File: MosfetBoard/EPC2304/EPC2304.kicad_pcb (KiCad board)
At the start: 2 copper layers, 120 x 75 mm, 179 parts, among them J10 DriverConn, J14 BATT-Conn2, J4 PhaseConn, J5 PhaseConn, J6 PhaseConn, J7 DriverConn, J8 DriverConn, J9 BATT-Conn1, Q1 EPC2304, Q13 EPC2304, Q14 EPC2304, Q15 EPC2304, Q2 EPC2304, Q3 EPC2304, Q4 EPC2304, Q5 EPC2304, Q6 EPC2304, Q7 EPC2304, Q8 EPC2304, Q9 EPC2304, U1 2EDF7275KXUMA1, U2 2EDF7275KXUMA1, U3 2EDF7275KXUMA1

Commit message: v2.6.2 - EPC2304
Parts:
- removed JP1, JP2, JP3: DummyJumper, GigaVescLibs:SolderJumper0.3mm
- added U10: INA181, Package_TO_SOT_SMD:SOT-23-6, F.Cu at (208.2, 108.2)
- added U11: INA181, Package_TO_SOT_SMD:SOT-23-6, F.Cu at (162.5, 108.2)
- added U12: INA181, Package_TO_SOT_SMD:SOT-23-6, F.Cu at (116.8, 108.2)
- R17, R18, R19, R28, R29, R30: footprint Resistor_SMD:R_1218_3246Metric_Pad1.22x4.75mm_HandSolder -> Resistor_SMD:R_2512_6332Metric
- moved C37 20.4 mm to (195.2, 101.0), turned to 180 degrees
- moved C38 20.4 mm to (149.5, 101.0), turned to 180 degrees
- moved C43 20.4 mm to (103.8, 101.0), turned to 180 degrees
- moved TH1 20.0 mm to (195.2, 99.5), turned to 0 degrees
- moved TH2 20.0 mm to (149.5, 99.5), turned to 0 degrees
- moved TH3 20.0 mm to (103.8, 99.5), turned to 0 degrees
- moved R15 18.5 mm to (103.8, 102.5), turned to 180 degrees
- moved R3 18.5 mm to (195.2, 102.5), turned to 180 degrees
- moved R4 18.5 mm to (149.5, 102.5), turned to 180 degrees
- moved R17 15.4 mm to (209.8, 103.2)
- moved R18 15.4 mm to (164.0, 103.2)
- moved R19 15.4 mm to (118.2, 103.2)
- moved C13 13.3 mm to (161.5, 60.8), turned to -90 degrees
- moved C17 13.3 mm to (115.8, 60.8), turned to -90 degrees
- moved C5 13.3 mm to (207.2, 60.8), turned to -90 degrees
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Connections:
- C14 pad 1: /PhaseMosfets2/3.3V_IN -> -BATT
- C14 pad 2: -BATT -> /PhaseMosfets2/3.3V_IN
- C18 pad 1: /PhaseMosfets3/3.3V_IN -> -BATT
- C18 pad 2: -BATT -> /PhaseMosfets3/3.3V_IN
- C6 pad 1: /PhaseMosfets1/3.3V_IN -> -BATT
- C6 pad 2: -BATT -> /PhaseMosfets1/3.3V_IN
- J4 pad 3: /PhaseMosfets1/SH- -> -BATT
- J5 pad 3: /PhaseMosfets2/SH- -> -BATT
- J6 pad 3: /PhaseMosfets3/SH- -> -BATT
- Q4 pad 2: /PhaseMosfets1/SH+ -> -BATT
- Q4 pad 4: /PhaseMosfets1/SH+ -> -BATT
- Q4 pad 6: /PhaseMosfets1/SH+ -> -BATT
- Q5 pad 2: /PhaseMosfets2/SH+ -> -BATT
- Q5 pad 4: /PhaseMosfets2/SH+ -> -BATT
- Q5 pad 6: /PhaseMosfets2/SH+ -> -BATT
- Q6 pad 2: /PhaseMosfets3/SH+ -> -BATT
- Q6 pad 4: /PhaseMosfets3/SH+ -> -BATT
- Q6 pad 6: /PhaseMosfets3/SH+ -> -BATT
- Q7 pad 2: /PhaseMosfets1/SH+ -> -BATT
- Q7 pad 4: /PhaseMosfets1/SH+ -> -BATT
- Q7 pad 6: /PhaseMosfets1/SH+ -> -BATT
- Q8 pad 2: /PhaseMosfets2/SH+ -> -BATT
- Q8 pad 4: /PhaseMosfets2/SH+ -> -BATT
- Q8 pad 6: /PhaseMosfets2/SH+ -> -BATT
- Q9 pad 2: /PhaseMosfets3/SH+ -> -BATT
- Q9 pad 4: /PhaseMosfets3/SH+ -> -BATT
- Q9 pad 6: /PhaseMosfets3/SH+ -> -BATT
- R17 pad 1: /PhaseMosfets1/SH+ -> /PhaseMosfets1/PHASE
- R17 pad 2: -BATT -> Net-(U10-+)
- R18 pad 1: /PhaseMosfets2/SH+ -> /PhaseMosfets2/PHASE
- R18 pad 2: -BATT -> Net-(U11-+)
- R19 pad 1: /PhaseMosfets3/SH+ -> /PhaseMosfets3/PHASE
- R19 pad 2: -BATT -> Net-(U12-+)
- R28 pad 1: /PhaseMosfets1/SH+ -> /PhaseMosfets1/PHASE
- R28 pad 2: -BATT -> Net-(U10-+)
- R29 pad 1: /PhaseMosfets2/SH+ -> /PhaseMosfets2/PHASE
- R29 pad 2: -BATT -> Net-(U11-+)
- R30 pad 1: /PhaseMosfets3/SH+ -> /PhaseMosfets3/PHASE
- R30 pad 2: -BATT -> Net-(U12-+)
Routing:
- net /PhaseMosfets3/3.3V_IN2: track 0.00 -> 35.3 mm
- net /PhaseMosfets3/PL: track 24.3 -> 3.41 mm
- net /PhaseMosfets3/12V_IN: track 15.9 -> 0.00 mm
- net -BATT: track 15.1 -> 0.00 mm
- net Net-(D15-A): track 1.38 -> 15.5 mm, vias 0 -> 2
- net /PhaseMosfets3/MOS_TEMP: track 0.00 -> 11.2 mm
- net /PhaseMosfets3/H: track 10.7 -> 0.00 mm
- net /PhaseMosfets3/DISABLE: track 10.7 -> 0.00 mm
- net /PhaseMosfets3/SH+: track 0.00 -> 9.76 mm
- net /PhaseMosfets3/3.3V_IN: track 7.52 -> 0.00 mm
- net Net-(D9-A): track 1.38 -> 7.52 mm, vias 0 -> 2
- net /PhaseMosfets3/V_SENSE: track 0.00 -> 6.10 mm
- net /PhaseMosfets3/L: track 5.74 -> 0.00 mm
- net Net-(D7-K): track 5.25 -> 0.00 mm
- net /PhaseMosfets3/PH: track 7.98 -> 4.00 mm
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- added copper zone on F.Cu, net Net-(U12-+)
- removed copper zone on F.Cu, net /PhaseMosfets3/SH+

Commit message: v2.7.0 - Phase shunts
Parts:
- removed U10, U11, U12: INA181, Package_TO_SOT_SMD:SOT-23-6
- added D16: 3.3V, Diode_SMD:D_MicroMELF, F.Cu at (192.5, 99.0)
- added D17: 3.3V, Diode_SMD:D_MicroMELF, F.Cu at (146.8, 99.0)
- added D18: 3.3V, Diode_SMD:D_MicroMELF, F.Cu at (101.0, 99.0)
- added R11: 10, Resistor_SMD:R_0603_1608Metric, F.Cu at (199.8, 101.5)
- added R12: 10, Resistor_SMD:R_0603_1608Metric, F.Cu at (154.0, 101.5)
- added R16: 10, Resistor_SMD:R_0603_1608Metric, F.Cu at (108.2, 101.5)
- added R31: 10, Resistor_SMD:R_0603_1608Metric, F.Cu at (189.5, 99.0)
- added R32: 10, Resistor_SMD:R_0603_1608Metric, F.Cu at (143.8, 99.0)
- added R33: 10, Resistor_SMD:R_0603_1608Metric, F.Cu at (98.0, 99.0)
- added U4: AMC1301DWVR, Package_SO:SOIC-8_7.5x5.85mm_P1.27mm, F.Cu at (191.5, 106.5)
- added U5: AMC1301DWVR, Package_SO:SOIC-8_7.5x5.85mm_P1.27mm, F.Cu at (145.8, 106.5)
- added U6: AMC1301DWVR, Package_SO:SOIC-8_7.5x5.85mm_P1.27mm, F.Cu at (100.0, 106.5)
- moved C37 1.60 mm to (196.2, 102.2)
- moved C38 1.60 mm to (150.5, 102.2)
- moved C43 1.60 mm to (104.8, 102.2)
- moved R15 1.60 mm to (104.8, 103.8)
- moved R3 1.60 mm to (196.2, 103.8)
- moved R4 1.60 mm to (150.5, 103.8)
- moved TH1 1.60 mm to (196.2, 100.8)
- moved TH2 1.60 mm to (150.5, 100.8)
- moved TH3 1.60 mm to (104.8, 100.8)
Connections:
- C15 pad 2: /PhaseMosfets2/PHASE -> GNDREF
- C19 pad 2: /PhaseMosfets3/PHASE -> GNDREF
- C7 pad 2: /PhaseMosfets1/PHASE -> GNDREF
- J4 pad 3: -BATT -> /PhaseMosfets1/SH-
- J5 pad 3: -BATT -> /PhaseMosfets2/SH-
- J6 pad 3: -BATT -> /PhaseMosfets3/SH-
- Q1 pad 2: /PhaseMosfets1/PHASE -> GNDREF
- Q1 pad 4: /PhaseMosfets1/PHASE -> GNDREF
- Q1 pad 6: /PhaseMosfets1/PHASE -> GNDREF
- Q13 pad 2: /PhaseMosfets1/PHASE -> GNDREF
- Q13 pad 4: /PhaseMosfets1/PHASE -> GNDREF
- Q13 pad 6: /PhaseMosfets1/PHASE -> GNDREF
- Q14 pad 2: /PhaseMosfets2/PHASE -> GNDREF
- Q14 pad 4: /PhaseMosfets2/PHASE -> GNDREF
- Q14 pad 6: /PhaseMosfets2/PHASE -> GNDREF
- Q15 pad 2: /PhaseMosfets3/PHASE -> GNDREF
- Q15 pad 4: /PhaseMosfets3/PHASE -> GNDREF
- Q15 pad 6: /PhaseMosfets3/PHASE -> GNDREF
- Q2 pad 2: /PhaseMosfets2/PHASE -> GNDREF
- Q2 pad 4: /PhaseMosfets2/PHASE -> GNDREF
- Q2 pad 6: /PhaseMosfets2/PHASE -> GNDREF
- Q3 pad 2: /PhaseMosfets3/PHASE -> GNDREF
- Q3 pad 4: /PhaseMosfets3/PHASE -> GNDREF
- Q3 pad 6: /PhaseMosfets3/PHASE -> GNDREF
- Q4 pad 3: /PhaseMosfets1/PHASE -> GNDREF
- Q4 pad 5: /PhaseMosfets1/PHASE -> GNDREF
- Q4 pad 7: /PhaseMosfets1/PHASE -> GNDREF
- Q5 pad 3: /PhaseMosfets2/PHASE -> GNDREF
- Q5 pad 5: /PhaseMosfets2/PHASE -> GNDREF
- Q5 pad 7: /PhaseMosfets2/PHASE -> GNDREF
- Q6 pad 3: /PhaseMosfets3/PHASE -> GNDREF
- Q6 pad 5: /PhaseMosfets3/PHASE -> GNDREF
- Q6 pad 7: /PhaseMosfets3/PHASE -> GNDREF
- Q7 pad 3: /PhaseMosfets1/PHASE -> GNDREF
- Q7 pad 5: /PhaseMosfets1/PHASE -> GNDREF
- Q7 pad 7: /PhaseMosfets1/PHASE -> GNDREF
- Q8 pad 3: /PhaseMosfets2/PHASE -> GNDREF
- Q8 pad 5: /PhaseMosfets2/PHASE -> GNDREF
- Q8 pad 7: /PhaseMosfets2/PHASE -> GNDREF
- Q9 pad 3: /PhaseMosfets3/PHASE -> GNDREF
- Q9 pad 5: /PhaseMosfets3/PHASE -> GNDREF
- Q9 pad 7: /PhaseMosfets3/PHASE -> GNDREF
- R1 pad 1: /PhaseMosfets1/PHASE -> GNDREF
- R13 pad 1: /PhaseMosfets2/PHASE -> GNDREF
- R17 pad 1: /PhaseMosfets1/PHASE -> GNDREF
- R18 pad 1: /PhaseMosfets2/PHASE -> GNDREF
- R19 pad 1: /PhaseMosfets3/PHASE -> GNDREF
- R20 pad 1: /PhaseMosfets3/PHASE -> GNDREF
- R27 pad 1: /PhaseMosfets1/PHASE -> GNDREF
- R28 pad 1: /PhaseMosfets1/PHASE -> GNDREF
- R29 pad 1: /PhaseMosfets2/PHASE -> GNDREF
- R30 pad 1: /PhaseMosfets3/PHASE -> GNDREF
- R40 pad 1: /PhaseMosfets2/PHASE -> GNDREF
- R47 pad 1: /PhaseMosfets3/PHASE -> GNDREF
- U1 pad 11: /PhaseMosfets1/PHASE -> GNDREF
- U2 pad 11: /PhaseMosfets2/PHASE -> GNDREF
- U3 pad 11: /PhaseMosfets3/PHASE -> GNDREF
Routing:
- net /PhaseMosfets3/3.3V_IN2: track 35.3 -> 5.80 mm
- net /PhaseMosfets3/SH-: track 0.00 -> 12.6 mm
- net GNDREF: track 0.00 -> 2.65 mm
- net /PhaseMosfets3/PHASE: track 2.65 -> 0.00 mm
- net /PhaseMosfets3/MOS_TEMP: track 11.2 -> 10.1 mm
- net /PhaseMosfets3/SH+: track 9.76 -> 10.3 mm
- added copper zone on F.Cu, net GNDREF
- removed copper zone on F.Cu, net /PhaseMosfets3/PHASE

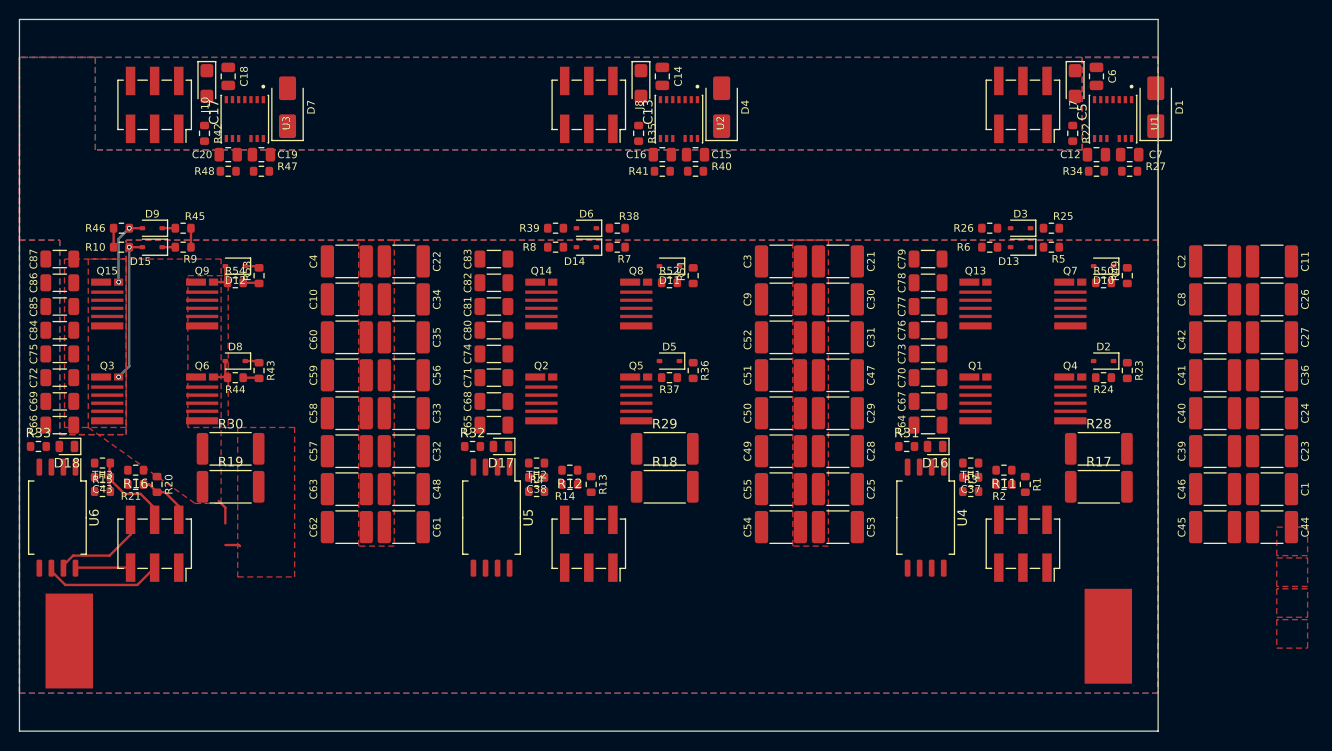
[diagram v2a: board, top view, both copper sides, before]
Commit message: v2.8.0 - Small Hall sensors
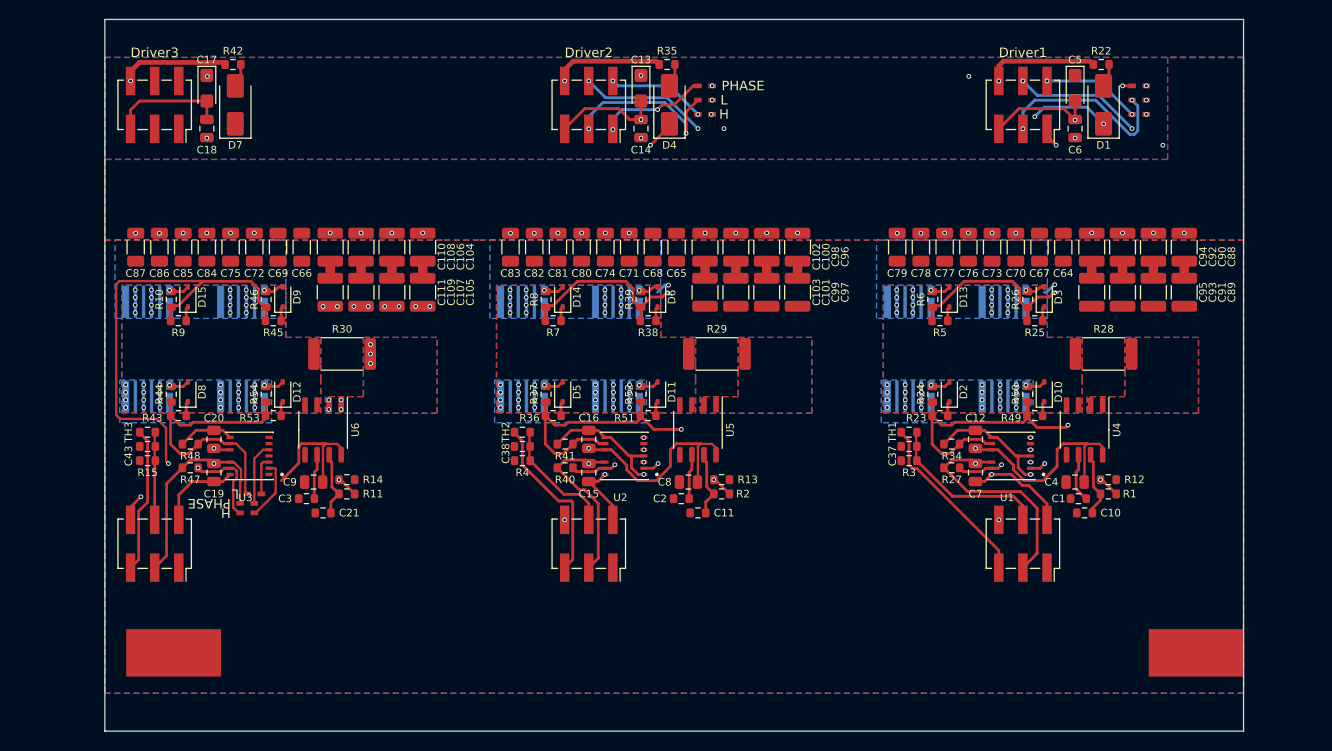
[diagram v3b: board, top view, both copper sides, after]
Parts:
- removed C22, C23, C24, C25, C26, C27, C28, C29, C30, C31, C32, C33, C34, C35, C36, C39, C40, C41, C42, C44, C45, C46, C47, C48, C49, C50, C51, C52, C53, C54, C55, C56, C57, C58, C59, C60, C61, C62, C63: 1u 200V, Capacitor_SMD:C_1812_4532Metric
- removed D16, D17, D18: 3.3V, Diode_SMD:D_MicroMELF
- removed R16, R31, R32, R33: 10, Resistor_SMD:R_0603_1608Metric
- removed R17, R18, R19: 0.5m, Resistor_SMD:R_2512_6332Metric
- removed R20: 150k, Resistor_SMD:R_0603_1608Metric
- removed R21: 2.7k, Resistor_SMD:R_0603_1608Metric
- added C100: 10u 100V, Capacitor_SMD:C_1210_3225Metric, F.Cu at (171.5, 78.0)
- added C101: 10u 100V, Capacitor_SMD:C_1210_3225Metric, F.Cu at (171.5, 82.8)
- added C102: 10u 100V, Capacitor_SMD:C_1210_3225Metric, F.Cu at (168.2, 78.0)
- added C103: 10u 100V, Capacitor_SMD:C_1210_3225Metric, F.Cu at (168.2, 82.8)
- added C104: 10u 100V, Capacitor_SMD:C_1210_3225Metric, F.Cu at (138.5, 78.0)
- added C105: 10u 100V, Capacitor_SMD:C_1210_3225Metric, F.Cu at (138.5, 82.8)
- added C106: 10u 100V, Capacitor_SMD:C_1210_3225Metric, F.Cu at (135.2, 78.0)
- added C107: 10u 100V, Capacitor_SMD:C_1210_3225Metric, F.Cu at (135.2, 82.8)
- added C108: 10u 100V, Capacitor_SMD:C_1210_3225Metric, F.Cu at (132.0, 78.0)
- added C109: 10u 100V, Capacitor_SMD:C_1210_3225Metric, F.Cu at (132.0, 82.8)
- added C110: 10u 100V, Capacitor_SMD:C_1210_3225Metric, F.Cu at (128.8, 78.0)
- added C111: 10u 100V, Capacitor_SMD:C_1210_3225Metric, F.Cu at (128.8, 82.8)
- added C88: 10u 100V, Capacitor_SMD:C_1210_3225Metric, F.Cu at (218.8, 78.0)
- added C89: 10u 100V, Capacitor_SMD:C_1210_3225Metric, F.Cu at (218.8, 82.8)
- added C90: 10u 100V, Capacitor_SMD:C_1210_3225Metric, F.Cu at (215.5, 78.0)
- added C91: 10u 100V, Capacitor_SMD:C_1210_3225Metric, F.Cu at (215.5, 82.8)
- added C92: 10u 100V, Capacitor_SMD:C_1210_3225Metric, F.Cu at (212.2, 78.0)
- added C93: 10u 100V, Capacitor_SMD:C_1210_3225Metric, F.Cu at (212.2, 82.8)
- added C94: 10u 100V, Capacitor_SMD:C_1210_3225Metric, F.Cu at (209.0, 78.0)
- added C95: 10u 100V, Capacitor_SMD:C_1210_3225Metric, F.Cu at (209.0, 82.8)
- added C96: 10u 100V, Capacitor_SMD:C_1210_3225Metric, F.Cu at (178.0, 78.0)
- added C97: 10u 100V, Capacitor_SMD:C_1210_3225Metric, F.Cu at (178.0, 82.8)
- added C98: 10u 100V, Capacitor_SMD:C_1210_3225Metric, F.Cu at (174.8, 78.0)
- added C99: 10u 100V, Capacitor_SMD:C_1210_3225Metric, F.Cu at (174.8, 82.8)
- added JP1: DirectJump, GigaVescLibs:SolderJumper0.5mm_Open, F.Cu at (214.0, 61.0)
- added JP10: DirectJump, GigaVescLibs:SolderJumper0.5mm_Open, F.Cu at (120.8, 104.0)
- added JP11: DirectJump, GigaVescLibs:SolderJumper0.5mm_Open, F.Cu at (120.0, 106.0)
- added JP2: DirectJump, GigaVescLibs:SolderJumper0.5mm_Open, F.Cu at (214.0, 62.5)
- added JP3: DirectJump, GigaVescLibs:SolderJumper0.5mm_Open, F.Cu at (214.0, 64.0)
- added JP5: DirectJump, GigaVescLibs:SolderJumper0.5mm_Open, F.Cu at (168.2, 61.0)
- added JP6: DirectJump, GigaVescLibs:SolderJumper0.5mm_Open, F.Cu at (168.2, 62.5)
- added JP7: DirectJump, GigaVescLibs:SolderJumper0.5mm_Open, F.Cu at (168.2, 64.0)
- added JP9: DirectJump, GigaVescLibs:SolderJumper0.5mm_Open, F.Cu at (120.0, 105.0)
- C1, C2, C3: value 1u 200V -> 10n; footprint Capacitor_SMD:C_1812_4532Metric -> GigaVescLibs:C_0603_1608Metric_L
- C10, C11, C21: value 1u 200V -> 1n; footprint Capacitor_SMD:C_1812_4532Metric -> GigaVescLibs:C_0603_1608Metric_L
- C4, C8, C9: value 1u 200V -> 100n; footprint Capacitor_SMD:C_1812_4532Metric -> Capacitor_SMD:C_0805_2012Metric
- Q1, Q13, Q14, Q15, Q2, Q3, Q4, Q5, Q6, Q7, Q8, Q9: moved to B.Cu
- R1: value 150k -> 4.7k
- R11: value 10 -> 4.7k
- R12: value 10 -> 9.1k
- R13: value 150k -> 9.1k
- R14: value 2.7k -> 9.1k
- R2: value 2.7k -> 4.7k
- R28, R29, R30: value 0.5m -> 0.3m
- U4, U5, U6: value AMC1301DWVR -> MT9223CT-50BR5; footprint Package_SO:SOIC-8_7.5x5.85mm_P1.27mm -> Package_SO:SOP-8_3.9x4.9mm_P1.27mm
- moved C10 80.9 mm to (208.2, 106.0)
- moved C4 80.2 mm to (207.2, 102.8), turned to 0 degrees
- moved R11 69.3 mm to (130.5, 104.0)
- moved C11 66.0 mm to (167.5, 106.0), turned to 180 degrees
- moved C2 61.6 mm to (165.8, 104.5)
- moved C21 60.4 mm to (128.0, 106.0), turned to 180 degrees
- moved C8 58.7 mm to (166.5, 102.8), turned to 0 degrees
- moved R12 56.8 mm to (210.8, 102.5)
- moved C3 55.9 mm to (126.2, 104.5)
- moved C9 52.9 mm to (127.0, 102.8), turned to 0 degrees
- moved C7 37.2 mm to (196.8, 101.8), turned to 90 degrees
- moved U1 37.1 mm to (200.5, 100.0), turned to 180 degrees
- moved R27 36.4 mm to (194.2, 101.2)
- moved U2 36.0 mm to (159.8, 100.0), turned to 180 degrees
- moved U3 35.5 mm to (120.2, 100.0), turned to 180 degrees
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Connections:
- C1 pad 1: +BATT -> Net-(U4-FILTER)
- C1 pad 2: -BATT -> GNDA
- C10 pad 1: +BATT -> Net-(U4-VIOUT)
- C10 pad 2: -BATT -> GNDA
- C11 pad 1: +BATT -> Net-(U5-VIOUT)
- C11 pad 2: -BATT -> GNDA
- C12 pad 1: /PhaseMosfets1/12V_IN -> /PhaseMosfets1/DRV_POWER
- C12 pad 2: /PhaseMosfets1/PHASE_GROUND -> -BATT
- C15 pad 1: Net-(D4-K) -> /PhaseMosfets2/FLOAT_VDD
- C15 pad 2: GNDREF -> /PhaseMosfets2/PHASE
- C16 pad 1: /PhaseMosfets2/12V_IN -> /PhaseMosfets2/DRV_POWER
- C16 pad 2: /PhaseMosfets2/PHASE_GROUND -> -BATT
- C19 pad 1: Net-(D7-K) -> /PhaseMosfets3/FLOAT_VDD
- C19 pad 2: GNDREF -> /PhaseMosfets3/PHASE
- C2 pad 1: +BATT -> Net-(U5-FILTER)
- C2 pad 2: -BATT -> GNDA
- C20 pad 1: /PhaseMosfets3/12V_IN -> /PhaseMosfets3/DRV_POWER
- C20 pad 2: /PhaseMosfets3/PHASE_GROUND -> -BATT
- C21 pad 1: +BATT -> Net-(U6-VIOUT)
- C21 pad 2: -BATT -> GNDA
- C3 pad 1: +BATT -> Net-(U6-FILTER)
- C3 pad 2: -BATT -> GNDA
- C4 pad 1: +BATT -> -BATT
- C4 pad 2: -BATT -> /PhaseMosfets1/DRV_POWER
- C7 pad 1: Net-(D1-K) -> /PhaseMosfets1/FLOAT_VDD
- C7 pad 2: GNDREF -> /PhaseMosfets1/PHASE
- C8 pad 1: +BATT -> -BATT
- C8 pad 2: -BATT -> /PhaseMosfets2/DRV_POWER
- C9 pad 1: +BATT -> -BATT
- C9 pad 2: -BATT -> /PhaseMosfets3/DRV_POWER
- D1 pad 1: Net-(D1-K) -> /PhaseMosfets1/FLOAT_VDD
- D4 pad 1: Net-(D4-K) -> /PhaseMosfets2/FLOAT_VDD
- D7 pad 1: Net-(D7-K) -> /PhaseMosfets3/FLOAT_VDD
- J10 pad 1: -BATT -> /PhaseMosfets3/LOCKOUT
- J10 pad 4: /PhaseMosfets3/DISABLE -> -BATT
- J10 pad 6: /PhaseMosfets3/12V_IN -> /PhaseMosfets3/DRV_POWER
- J4 pad 2: /PhaseMosfets1/V_SENSE -> /PhaseMosfets1/FLOAT_VDD
- J4 pad 3: /PhaseMosfets1/SH- -> GNDA
- J5 pad 2: /PhaseMosfets2/V_SENSE -> /PhaseMosfets2/FLOAT_VDD
- J5 pad 3: /PhaseMosfets2/SH- -> GNDA
- J6 pad 2: /PhaseMosfets3/V_SENSE -> /PhaseMosfets3/FLOAT_VDD
- J6 pad 3: /PhaseMosfets3/SH- -> GNDA
- J7 pad 1: -BATT -> /PhaseMosfets1/LOCKOUT
- J7 pad 4: /PhaseMosfets1/DISABLE -> -BATT
- J7 pad 6: /PhaseMosfets1/12V_IN -> /PhaseMosfets1/DRV_POWER
- J8 pad 1: -BATT -> /PhaseMosfets2/LOCKOUT
- J8 pad 4: /PhaseMosfets2/DISABLE -> -BATT
- J8 pad 6: /PhaseMosfets2/12V_IN -> /PhaseMosfets2/DRV_POWER
- Q1 pad 2: GNDREF -> /PhaseMosfets1/PHASE
- Q1 pad 4: GNDREF -> /PhaseMosfets1/PHASE
- Q1 pad 6: GNDREF -> /PhaseMosfets1/PHASE
- Q13 pad 2: GNDREF -> /PhaseMosfets1/PHASE
- Q13 pad 4: GNDREF -> /PhaseMosfets1/PHASE
- Q13 pad 6: GNDREF -> /PhaseMosfets1/PHASE
- Q14 pad 2: GNDREF -> /PhaseMosfets2/PHASE
- Q14 pad 4: GNDREF -> /PhaseMosfets2/PHASE
- Q14 pad 6: GNDREF -> /PhaseMosfets2/PHASE
- Q15 pad 2: GNDREF -> /PhaseMosfets3/PHASE
- Q15 pad 4: GNDREF -> /PhaseMosfets3/PHASE
- Q15 pad 6: GNDREF -> /PhaseMosfets3/PHASE
- Q2 pad 2: GNDREF -> /PhaseMosfets2/PHASE
- Q2 pad 4: GNDREF -> /PhaseMosfets2/PHASE
- Q2 pad 6: GNDREF -> /PhaseMosfets2/PHASE
- Q3 pad 2: GNDREF -> /PhaseMosfets3/PHASE
- Q3 pad 4: GNDREF -> /PhaseMosfets3/PHASE
- Q3 pad 6: GNDREF -> /PhaseMosfets3/PHASE
- Q4 pad 3: GNDREF -> /PhaseMosfets1/PHASE
- Q4 pad 5: GNDREF -> /PhaseMosfets1/PHASE
- Q4 pad 7: GNDREF -> /PhaseMosfets1/PHASE
- Q5 pad 3: GNDREF -> /PhaseMosfets2/PHASE
- Q5 pad 5: GNDREF -> /PhaseMosfets2/PHASE
- Q5 pad 7: GNDREF -> /PhaseMosfets2/PHASE
- Q6 pad 3: GNDREF -> /PhaseMosfets3/PHASE
- Q6 pad 5: GNDREF -> /PhaseMosfets3/PHASE
- Q6 pad 7: GNDREF -> /PhaseMosfets3/PHASE
- Q7 pad 3: GNDREF -> /PhaseMosfets1/PHASE
- Q7 pad 5: GNDREF -> /PhaseMosfets1/PHASE
- Q7 pad 7: GNDREF -> /PhaseMosfets1/PHASE
- Q8 pad 3: GNDREF -> /PhaseMosfets2/PHASE
- Q8 pad 5: GNDREF -> /PhaseMosfets2/PHASE
- Q8 pad 7: GNDREF -> /PhaseMosfets2/PHASE
- Q9 pad 3: GNDREF -> /PhaseMosfets3/PHASE
- Q9 pad 5: GNDREF -> /PhaseMosfets3/PHASE
- Q9 pad 7: GNDREF -> /PhaseMosfets3/PHASE
- R1 pad 1: GNDREF -> /PhaseMosfets1/SH+
- R1 pad 2: /PhaseMosfets1/V_SENSE -> Net-(U4-VIOUT)
- R11 pad 1: Net-(R11-Pad1) -> /PhaseMosfets3/SH+
- R11 pad 2: Net-(R11-Pad2) -> Net-(U6-VIOUT)
- R12 pad 1: Net-(R12-Pad1) -> GNDA
- R12 pad 2: Net-(R12-Pad2) -> /PhaseMosfets1/SH+
- R13 pad 1: GNDREF -> GNDA
- R13 pad 2: /PhaseMosfets2/V_SENSE -> /PhaseMosfets2/SH+
- R14 pad 1: /PhaseMosfets2/V_SENSE -> GNDA
- R14 pad 2: -BATT -> /PhaseMosfets3/SH+
- R2 pad 1: /PhaseMosfets1/V_SENSE -> /PhaseMosfets2/SH+
- R2 pad 2: -BATT -> Net-(U5-VIOUT)
- R22 pad 1: /PhaseMosfets1/12V_IN -> /PhaseMosfets1/DRV_POWER
- R27 pad 1: GNDREF -> /PhaseMosfets1/PHASE
- R28 pad 1: GNDREF -> /PhaseMosfets1/PHASE
- R28 pad 2: Net-(R11-Pad1) -> Net-(R28-Pad2)
- R29 pad 1: GNDREF -> /PhaseMosfets2/PHASE
- R29 pad 2: Net-(R12-Pad1) -> Net-(R29-Pad2)
- R30 pad 1: GNDREF -> /PhaseMosfets3/PHASE
- R30 pad 2: Net-(R16-Pad1) -> Net-(R30-Pad2)
- R34 pad 1: /PhaseMosfets1/PHASE_GROUND -> -BATT
- R35 pad 1: /PhaseMosfets2/12V_IN -> /PhaseMosfets2/DRV_POWER
- R40 pad 1: GNDREF -> /PhaseMosfets2/PHASE
- R41 pad 1: /PhaseMosfets2/PHASE_GROUND -> -BATT
- R42 pad 1: /PhaseMosfets3/12V_IN -> /PhaseMosfets3/DRV_POWER
- R47 pad 1: GNDREF -> /PhaseMosfets3/PHASE
- R48 pad 1: /PhaseMosfets3/PHASE_GROUND -> -BATT
- U1 pad 10: /PhaseMosfets1/12V_IN -> /PhaseMosfets1/DRV_POWER
- U1 pad 11: GNDREF -> /PhaseMosfets1/PHASE
- U1 pad 13: Net-(D1-K) -> /PhaseMosfets1/FLOAT_VDD
- U1 pad 5: /PhaseMosfets1/DISABLE -> /PhaseMosfets1/LOCKOUT
- U1 pad 8: /PhaseMosfets1/PHASE_GROUND -> -BATT
- U2 pad 10: /PhaseMosfets2/12V_IN -> /PhaseMosfets2/DRV_POWER
- U2 pad 11: GNDREF -> /PhaseMosfets2/PHASE
- U2 pad 13: Net-(D4-K) -> /PhaseMosfets2/FLOAT_VDD
- U2 pad 5: /PhaseMosfets2/DISABLE -> /PhaseMosfets2/LOCKOUT
- U2 pad 8: /PhaseMosfets2/PHASE_GROUND -> -BATT
- U3 pad 10: /PhaseMosfets3/12V_IN -> /PhaseMosfets3/DRV_POWER
- U3 pad 11: GNDREF -> /PhaseMosfets3/PHASE
- U3 pad 13: Net-(D7-K) -> /PhaseMosfets3/FLOAT_VDD
- U3 pad 5: /PhaseMosfets3/DISABLE -> /PhaseMosfets3/LOCKOUT
- U3 pad 8: /PhaseMosfets3/PHASE_GROUND -> -BATT
- U4 pad 1: Net-(D16-K) -> Net-(R28-Pad2)
- U4 pad 2: Net-(R11-Pad2) -> Net-(R28-Pad2)
- U4 pad 3: Net-(R31-Pad2) -> /PhaseMosfets1/PHASE
- U4 pad 4: GNDREF -> /PhaseMosfets1/PHASE
- U4 pad 5: -BATT -> GNDA
- U4 pad 6: /PhaseMosfets1/SH- -> Net-(U4-FILTER)
- U4 pad 7: /PhaseMosfets1/SH+ -> Net-(U4-VIOUT)
- U4 pad 8: /PhaseMosfets1/3.3V_IN2 -> /PhaseMosfets1/DRV_POWER
- U5 pad 1: Net-(D17-K) -> Net-(R29-Pad2)
- U5 pad 2: Net-(R12-Pad2) -> Net-(R29-Pad2)
- U5 pad 3: Net-(R32-Pad2) -> /PhaseMosfets2/PHASE
- U5 pad 4: GNDREF -> /PhaseMosfets2/PHASE
- U5 pad 5: -BATT -> GNDA
- U5 pad 6: /PhaseMosfets2/SH- -> Net-(U5-FILTER)
- U5 pad 7: /PhaseMosfets2/SH+ -> Net-(U5-VIOUT)
- U5 pad 8: /PhaseMosfets2/3.3V_IN2 -> /PhaseMosfets2/DRV_POWER
- U6 pad 1: Net-(D18-K) -> Net-(R30-Pad2)
- U6 pad 2: Net-(R16-Pad2) -> Net-(R30-Pad2)
- U6 pad 3: Net-(R33-Pad2) -> /PhaseMosfets3/PHASE
- U6 pad 4: GNDREF -> /PhaseMosfets3/PHASE
- U6 pad 5: -BATT -> GNDA
- U6 pad 6: /PhaseMosfets3/SH- -> Net-(U6-FILTER)
- U6 pad 7: /PhaseMosfets3/SH+ -> Net-(U6-VIOUT)
- U6 pad 8: /PhaseMosfets3/3.3V_IN2 -> /PhaseMosfets3/DRV_POWER
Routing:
- net -BATT: track 0.00 -> 143.0 mm, vias 0 -> 22
- net /PhaseMosfets1/DRV_POWER: track 0.00 -> 88.4 mm, vias 0 -> 2
- net /PhaseMosfets2/DRV_POWER: track 0.00 -> 85.8 mm, vias 0 -> 2
- net /PhaseMosfets3/DRV_POWER: track 0.00 -> 75.6 mm, vias 0 -> 2
- net /PhaseMosfets1/PH: track 0.00 -> 73.2 mm, vias 0 -> 3
- net /PhaseMosfets2/PH: track 0.00 -> 68.7 mm, vias 0 -> 3
- net /PhaseMosfets1/PL: track 0.00 -> 68.3 mm, vias 0 -> 2
- net /PhaseMosfets2/PL: track 0.00 -> 65.9 mm, vias 0 -> 2
- net /PhaseMosfets1/L: track 0.00 -> 62.6 mm, vias 0 -> 3
- net /PhaseMosfets1/FLOAT_VDD: track 0.00 -> 59.1 mm, vias 0 -> 3
- net /PhaseMosfets1/PHASE: track 0.00 -> 57.6 mm, vias 0 -> 43
- net /PhaseMosfets3/PH: track 4.00 -> 61.2 mm, vias 0 -> 2
- net /PhaseMosfets2/L: track 0.00 -> 55.1 mm, vias 0 -> 3
- net /PhaseMosfets1/H: track 0.00 -> 53.6 mm, vias 0 -> 3
- net /PhaseMosfets2/H: track 0.00 -> 51.3 mm, vias 0 -> 3
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- added copper zone on In1.Cu, net +BATT
- added copper zone on In1.Cu, net -BATT
- added copper zone on In2.Cu, net -BATT
- added copper zone on B.Cu, net /PhaseMosfets1/PHASE
- added copper zone on F.Cu, net /PhaseMosfets1/PHASE
- added copper zone on In1.Cu, net /PhaseMosfets1/PHASE
- added copper zone on In2.Cu, net /PhaseMosfets1/PHASE
- added copper zone on B.Cu, net /PhaseMosfets2/PHASE
- added copper zone on F.Cu, net /PhaseMosfets2/PHASE
- added copper zone on In1.Cu, net /PhaseMosfets2/PHASE
- added copper zone on In2.Cu, net /PhaseMosfets2/PHASE
- added copper zone on B.Cu, net /PhaseMosfets3/PHASE
- added copper zone on F.Cu, net /PhaseMosfets3/PHASE
- added copper zone on In1.Cu, net /PhaseMosfets3/PHASE
- added copper zone on In2.Cu, net /PhaseMosfets3/PHASE
- added copper zone on B.Cu, net Net-(R28-Pad2)
- added copper zone on F.Cu, net Net-(R28-Pad2)
- added copper zone on In1.Cu, net Net-(R28-Pad2)
- added copper zone on In2.Cu, net Net-(R28-Pad2)
- added copper zone on B.Cu, net Net-(R29-Pad2)
- added copper zone on F.Cu, net Net-(R29-Pad2)
- added copper zone on In1.Cu, net Net-(R29-Pad2)
- added copper zone on In2.Cu, net Net-(R29-Pad2)
- added copper zone on B.Cu, net Net-(R30-Pad2)
- added copper zone on F.Cu, net Net-(R30-Pad2)
- added copper zone on In1.Cu, net Net-(R30-Pad2)
- added copper zone on In2.Cu, net Net-(R30-Pad2)
- removed copper zone on F.Cu, net GNDREF
- removed copper zone on F.Cu, net Net-(R16-Pad1)
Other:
- copper layers 2 -> 4
